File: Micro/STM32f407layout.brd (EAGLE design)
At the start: 100.1 x 96.7 mm, 69 parts, among them Q1 ASF, T3 FDN340P, T4 AP1117_LIN_REG

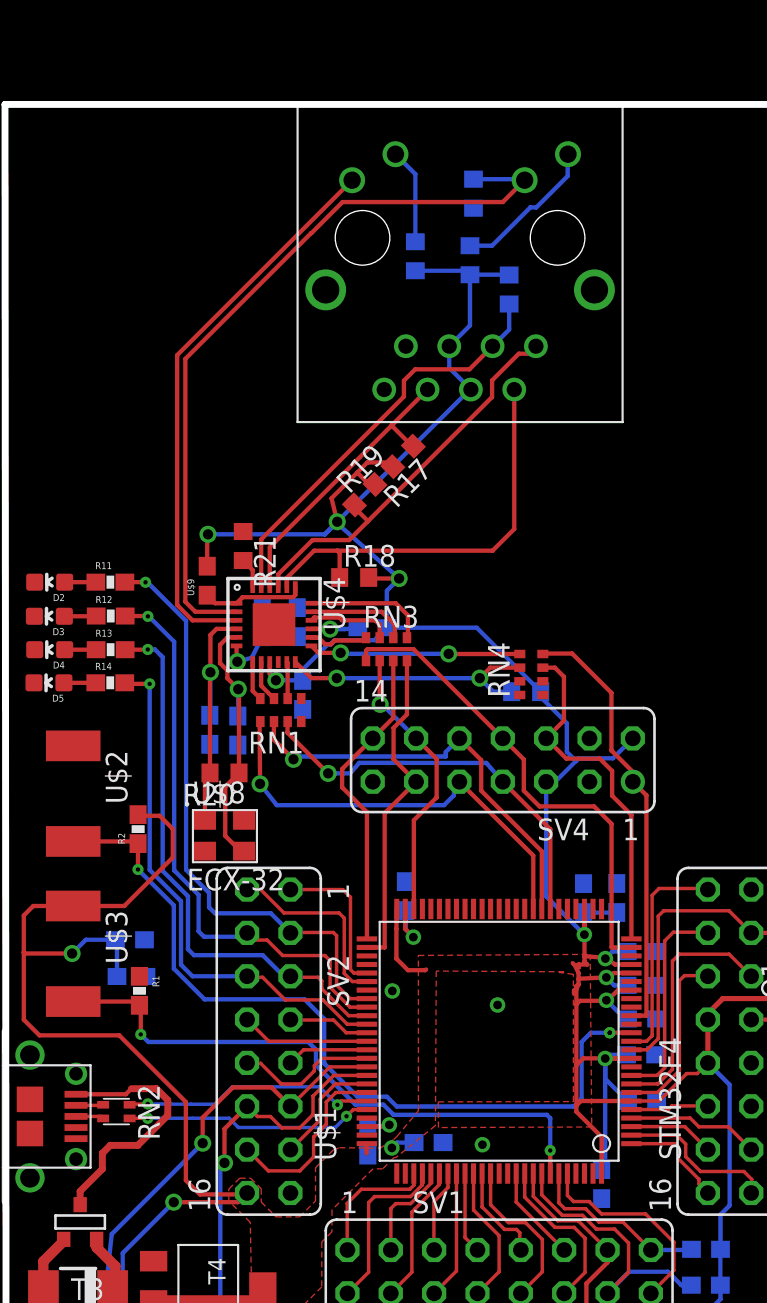
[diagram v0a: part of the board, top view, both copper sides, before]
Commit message: More Updates
Moved ehternet jack, made things similar in length
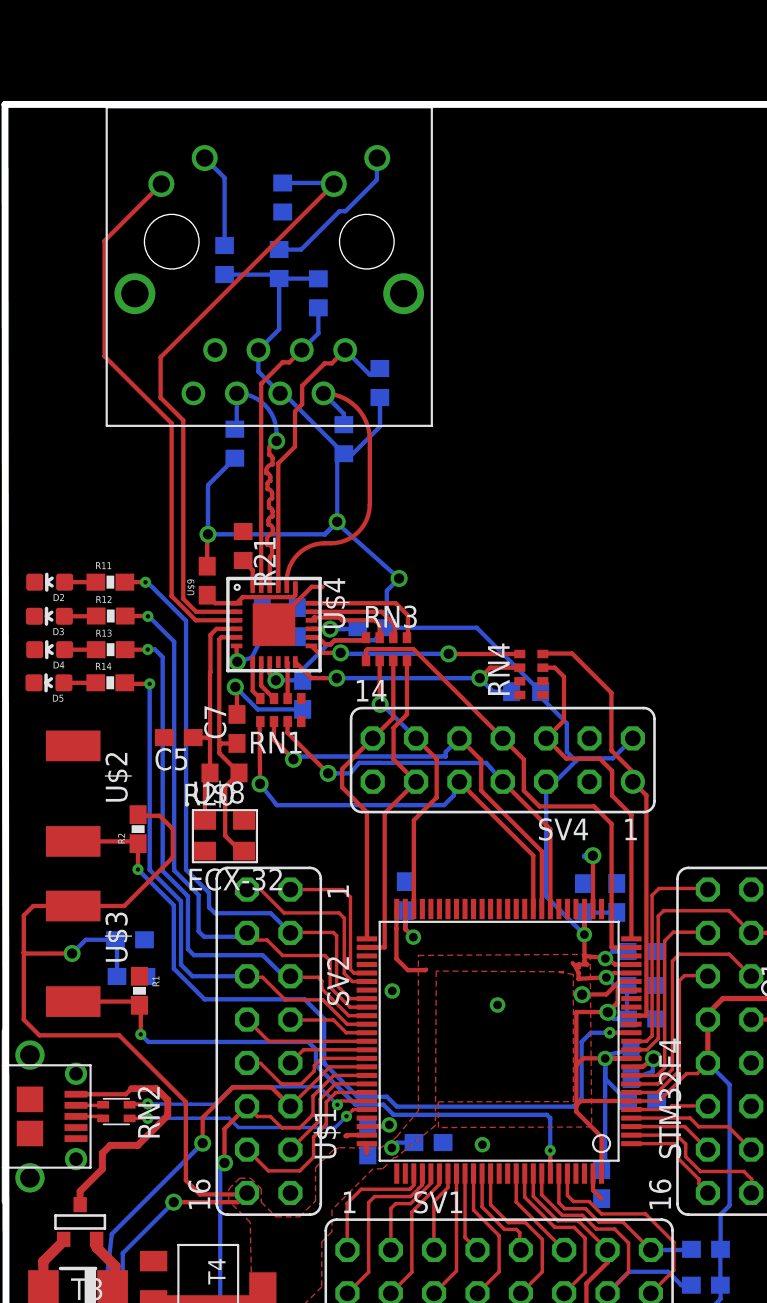
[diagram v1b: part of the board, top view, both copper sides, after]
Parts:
- moved R15 11.2 mm to (38.3, 71.3)
- moved U$7 11.2 mm to (44.1, 63.5)
- moved R16 11.2 mm to (43.8, 69.4)
- moved R22 11.2 mm to (41.7, 75.0)
- moved R7 11.2 mm to (41.5, 71.1)
- moved R17 9.89 mm to (38.9, 60.6), flipped to the bottom, turned to 270 degrees
- moved R18 8.13 mm to (45.3, 60.8), flipped to the bottom, turned to 270 degrees
- moved R19 6.60 mm to (47.4, 64.1), flipped to the bottom, turned to 270 degrees
- moved C5 1.88 mm to (35.6, 43.3), flipped to the top, turned to 180 degrees
- moved C6 0.81 mm to (62.1, 24.2), turned to 270 degrees
- moved C7 0.11 mm to (39.0, 43.8), flipped to the top, turned to 90 degrees
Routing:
- net GND: track 15.3 -> 39.1 mm, vias 1 -> 5
- net BUS_SPEED: track 44.7 -> 35.5 mm
- net TD-: track 24.8 -> 17.2 mm
- net RD+: track 24.5 -> 18.0 mm
- net TD+: track 23.2 -> 18.5 mm
- net +3V3: track 279.3 -> 281.2 mm, vias 14 -> 15
- net XTAL2: track 15.2 -> 13.7 mm, vias 1 -> 0
- net LINK/ACT: track 33.0 -> 31.5 mm
- net RD-: track 17.2 -> 16.0 mm, vias 0 -> 1
- net XTAL1: track 16.3 -> 16.1 mm, vias 1 -> 0

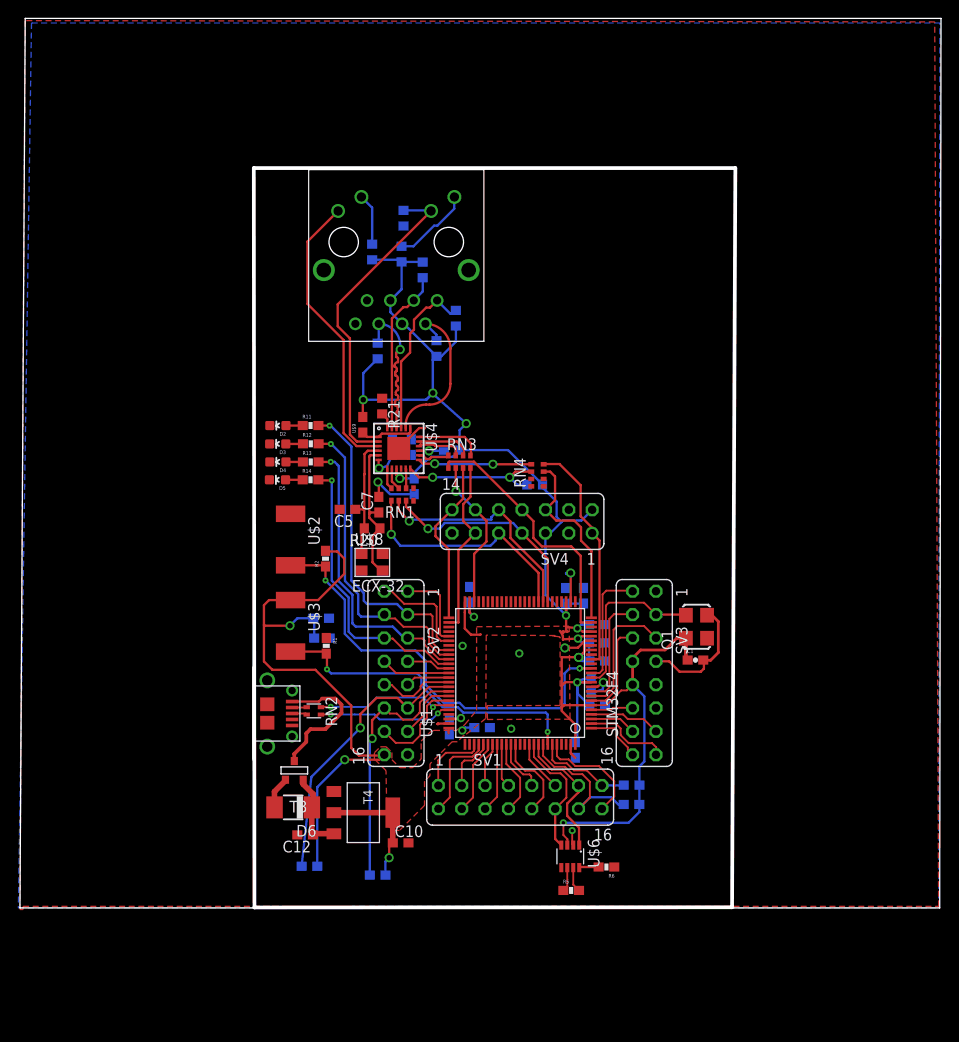
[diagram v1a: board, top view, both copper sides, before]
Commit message: Other Update
Updated power and ground, might need more fixing based on other traces.
need to check if can use different pins for Sonar PWM and DAC, as well
as Servo PWMs.
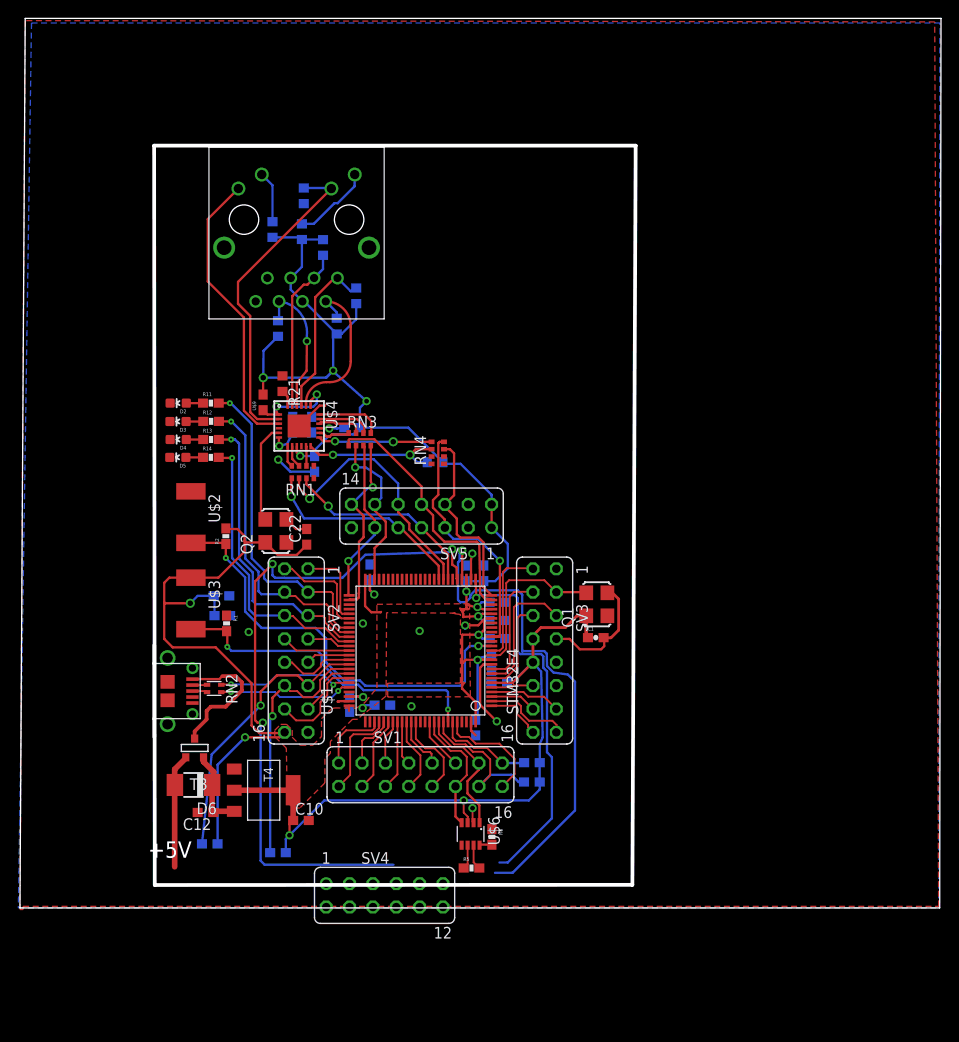
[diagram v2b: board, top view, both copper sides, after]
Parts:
- removed C5, C7: 22pF, eagle-ltspice:C0603
- removed R20: 1M, resistor:R0603
- removed U$8: ECX-32, Other:ECX-32
- added C22: 0.01uF, resistor:C0603
- added Q2: ASV-8, MicroBoard:ASF
- added SV5: (no value), con-lsta:FE07-2
- SV4: device con-lsta:FE07-2 -> con-lsta:FE06-2
- moved SV4 43.3 mm to (39.6, 1.36), turned to 0 degrees
- moved R6 12.9 mm to (51.3, 7.72), turned to 270 degrees
- moved C4 11.1 mm to (48.5, 36.4)
- moved Q1 11.1 mm to (62.7, 33.0)
- moved R8 11.1 mm to (36.1, 52.2)
- moved RN3 11.1 mm to (36.9, 51.0)
- moved SV3 11.1 mm to (57.0, 28.0)
- moved C20 11.1 mm to (21.9, 33.9)
- moved R2 11.1 mm to (22.4, 40.4)
- moved U$4 11.1 mm to (30.4, 52.4)
- moved D4 11.1 mm to (17.2, 50.9)
- moved R12 11.1 mm to (20.8, 52.9)
- moved R13 11.1 mm to (20.8, 50.9)
- moved R4 11.1 mm to (20.6, 6.96)
- moved T3 11.1 mm to (19.0, 17.4)
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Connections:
- net +3V3: now also C22.1, Q2.4, SV5.1, SV5.2; no longer SV4.2, SV4.5
- net +5V: now also SV4.1
- net ALT_CAMERA_SERVO_MOTOR_PWM: now also SV4.12
- net CANH1: now also SV4.3
- net CANL1: now also SV4.4
- net CRS_DV: now also SV5.7; no longer SV4.7
- net GND: now also C22.2, Q2.2, SV4.2, SV5.3, SV5.4; no longer C5.2, C7.2, SV4.3, SV4.4, U$8.GND, U$8.GND2
- net I2C1_SCL: now also SV4.5
- net I2C1_SDA: now also SV4.6
- net I2C3_SCL: now also SV4.9
- net I2C3_SDA: now also SV4.10
- net MAIN_CAMERA_SERVO_MOTOR_PWM: now also SV4.11
- net MDC: now also SV5.5; no longer SV4.1
- net MDIO: now also SV5.6; no longer SV4.6
- net REFCLK: now also SV5.8; no longer SV4.8
- net RXD0: now also SV5.10; no longer SV4.10
- net RXD1: now also SV5.9; no longer SV4.9
- net SONAR_DAC: now also SV4.8
- net SONAR_PWM: now also SV4.7
- net TXD0: now also SV5.11; no longer SV4.14
- net TXD1: now also SV5.14; no longer SV4.11
- net TXEN: now also SV5.12; no longer SV4.12
- net XTAL1: now also Q2.3; no longer C7.1, R20.1, U$8.OUT/IN
- net XTAL2: no longer C5.1, R20.2, U$8.IN/OUT
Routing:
- net SONAR_PWM: track 0.00 -> 74.1 mm, vias 0 -> 3
- net SONAR_DAC: track 0.00 -> 56.2 mm, vias 0 -> 1
- net ALT_CAMERA_SERVO_MOTOR_PWM: track 0.00 -> 41.5 mm, vias 0 -> 1
- net +3V3: track 281.2 -> 301.9 mm, vias 15 -> 14
- net XTAL2: track 13.7 -> 0.00 mm
- net +5V: track 3.51 -> 12.4 mm
- net XTAL1: track 16.1 -> 10.9 mm
- net GND: track 39.1 -> 43.4 mm, vias 5 -> 6
- net N$21: track 6.02 -> 9.98 mm, vias 0 -> 2
- net RXD1: track 26.0 -> 23.0 mm
- net RXD0: track 25.1 -> 27.8 mm
- net MDC: track 25.6 -> 28.3 mm, vias 0 -> 1
- net CRS_DV: track 23.7 -> 22.1 mm
- net TXEN: track 16.6 -> 17.9 mm
- net RD-: track 16.0 -> 15.2 mm
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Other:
- outline, holes or cut-outs redrawn
- board text added: "+5V"

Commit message: Added rough sketch for bottom pinout
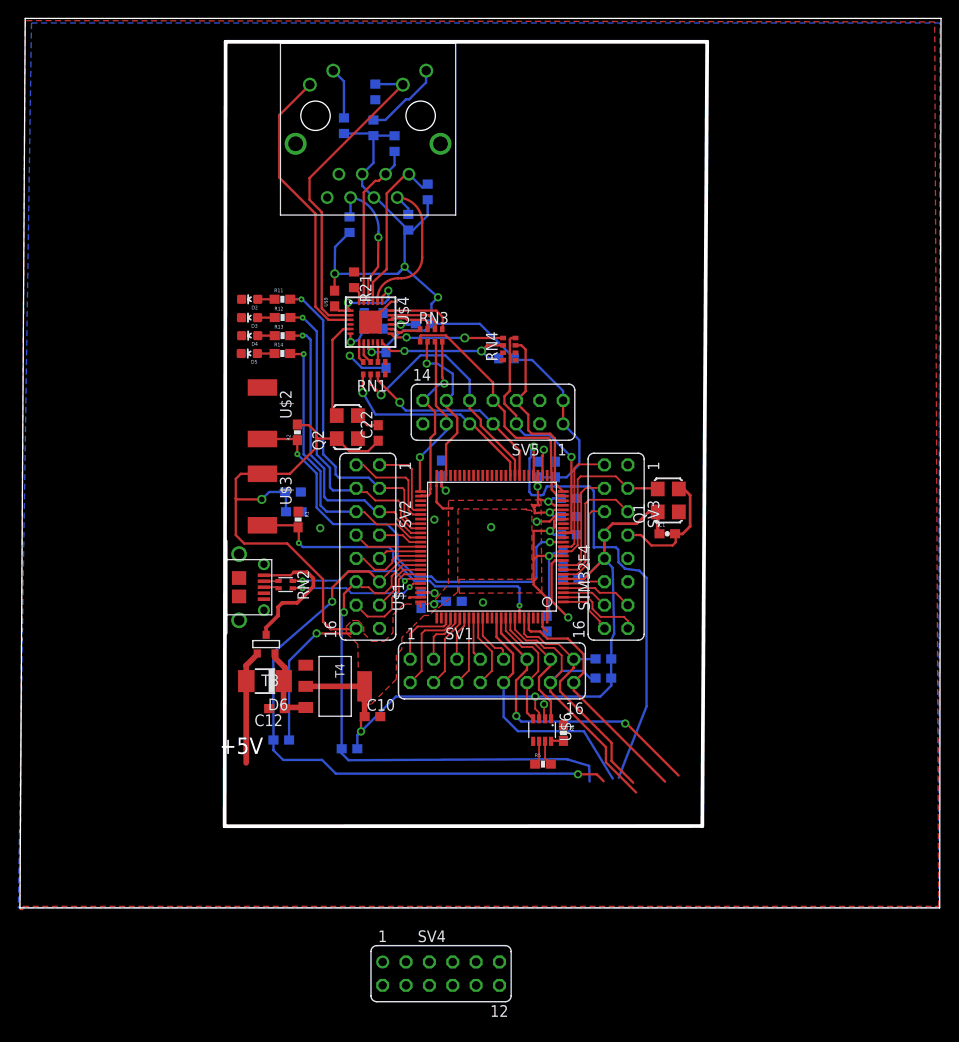
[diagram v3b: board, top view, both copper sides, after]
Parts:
- moved R7 13.7 mm to (38.4, 84.8)
- moved C15 13.7 mm to (37.4, 63.8)
- moved C3 13.7 mm to (45.8, 47.8)
- moved D4 13.7 mm to (25.0, 62.2)
- moved D5 13.7 mm to (24.9, 60.3)
- moved R11 13.7 mm to (28.5, 66.2)
- moved R13 13.7 mm to (28.6, 62.2)
- moved R17 13.7 mm to (35.8, 74.3)
- moved R18 13.7 mm to (42.2, 74.6)
- moved R8 13.7 mm to (43.9, 63.5)
- moved RN3 13.7 mm to (44.7, 62.2)
- moved SV5 13.7 mm to (51.4, 53.9)
- moved U$2 13.7 mm to (26.4, 53.8)
- moved R23 13.7 mm to (52.9, 59.8)
- moved C10 13.7 mm to (38.3, 20.8)
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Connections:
- removed net PB3: U$1.P89
- removed net PB4: SV1.11, U$1.P90
- removed net PB9: SV1.16, U$1.P96
- new net PA0: U$1.P23
- new net PA3: U$1.P26
- new net PA6: U$1.P31
- net ALT_CAMERA_SERVO_MOTOR_PWM: now also SV1.16, U$1.P96; no longer U$1.P26
- net MAIN_CAMERA_SERVO_MOTOR_PWM: now also SV1.11, U$1.P90; no longer U$1.P23
- net PA5: now also U$1.P30; no longer U$1.P31
- net PD6: no longer SV1.10
- net SONAR_PWM: now also SV1.10, U$1.P89; no longer U$1.P30
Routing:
- net SONAR_PWM: track 74.1 -> 27.3 mm, vias 3 -> 0
- net I2C3_SDA: track 30.6 -> 69.6 mm, vias 1 -> 2
- net MAIN_CAMERA_SERVO_MOTOR_PWM: track 0.00 -> 32.7 mm, vias 0 -> 2
- net I2C3_SCL: track 28.3 -> 57.8 mm
- net I2C1_SCL: track 10.6 -> 28.0 mm
- net I2C1_SDA: track 16.7 -> 32.5 mm
- net ALT_CAMERA_SERVO_MOTOR_PWM: track 41.5 -> 26.7 mm, vias 1 -> 0
- net PB9: track 12.2 -> 0.00 mm
- net PD6: track 9.38 -> 0.00 mm
- net PB4: track 5.64 -> 0.00 mm
- net SONAR_DAC: track 56.2 -> 52.5 mm
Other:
- outline, holes or cut-outs redrawn

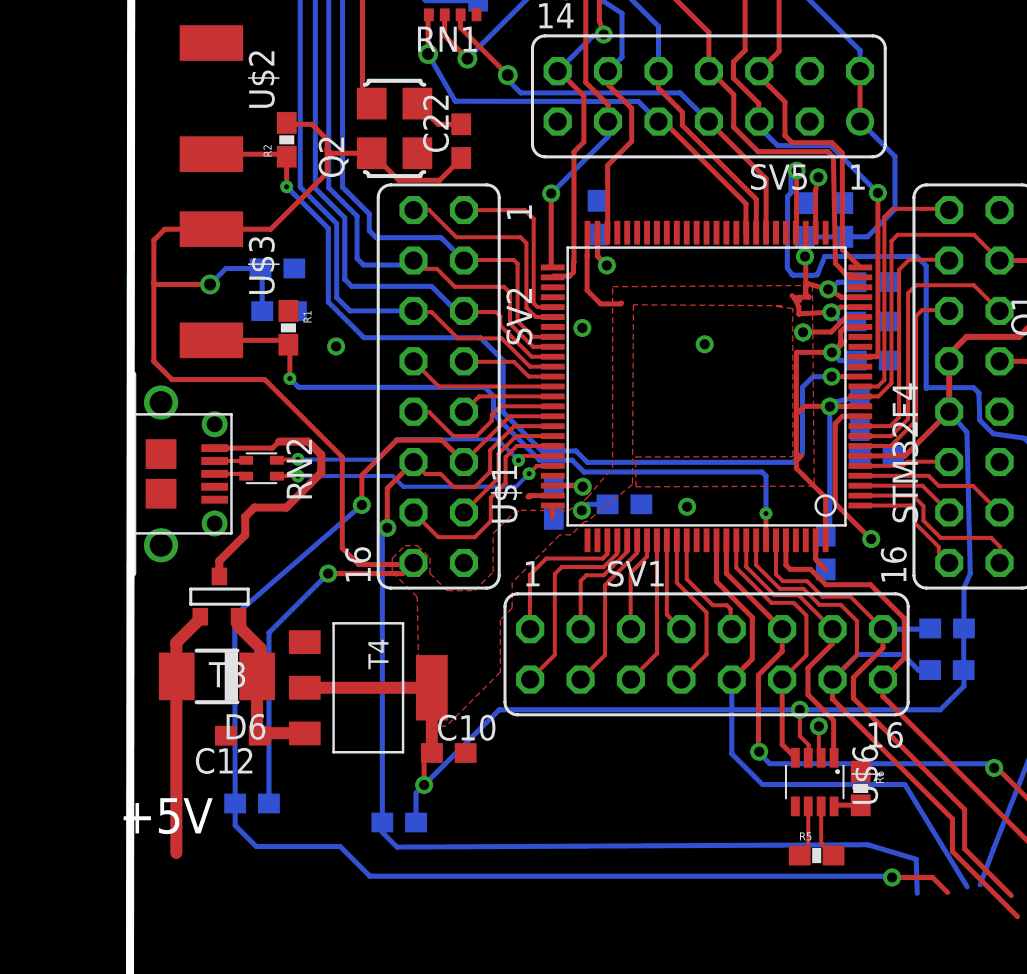
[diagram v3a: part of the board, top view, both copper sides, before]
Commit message: Fixed Polygons for Power and GND
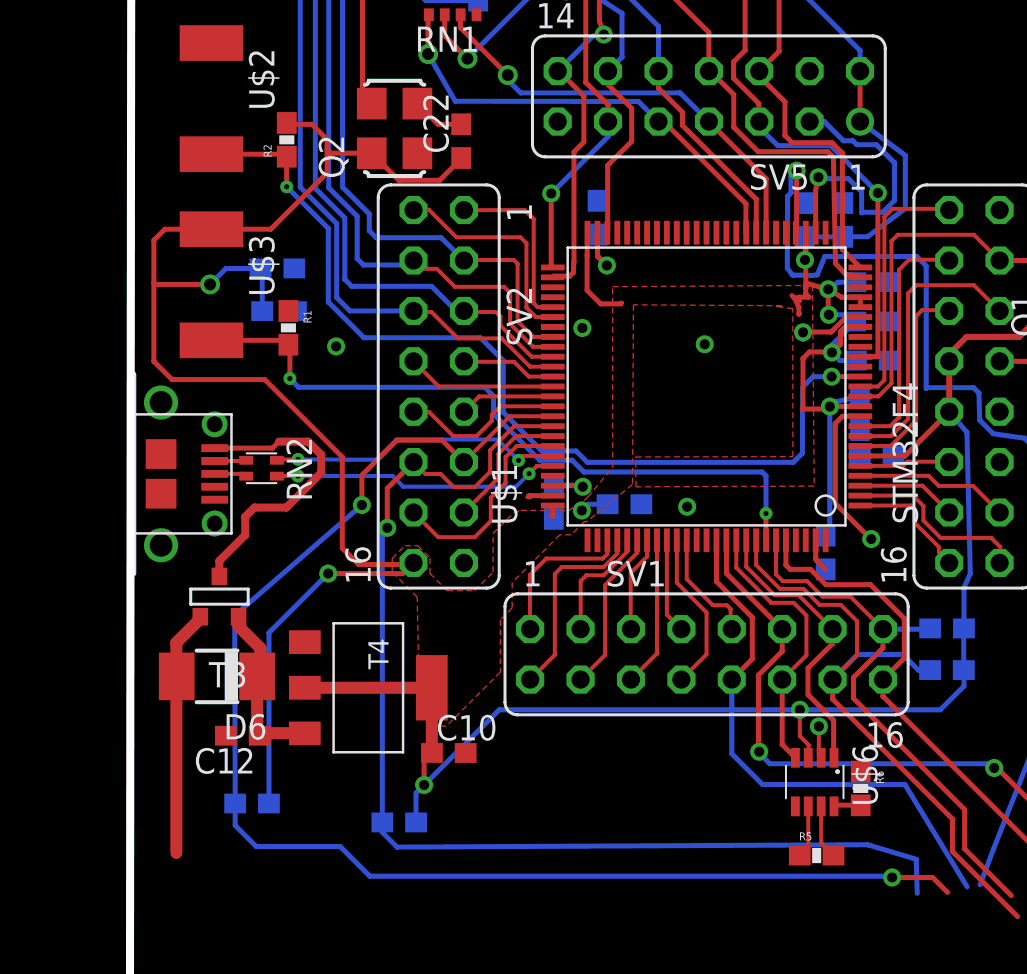
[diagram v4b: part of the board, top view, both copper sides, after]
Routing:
- net GND: track 43.4 -> 55.9 mm
- net +3V3: track 302.2 -> 294.3 mm
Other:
- board text removed: "+5V"
